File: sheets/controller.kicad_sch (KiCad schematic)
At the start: 40 parts, among them CN1 CTRL1, CN2 CTRL2, U12 74LS06

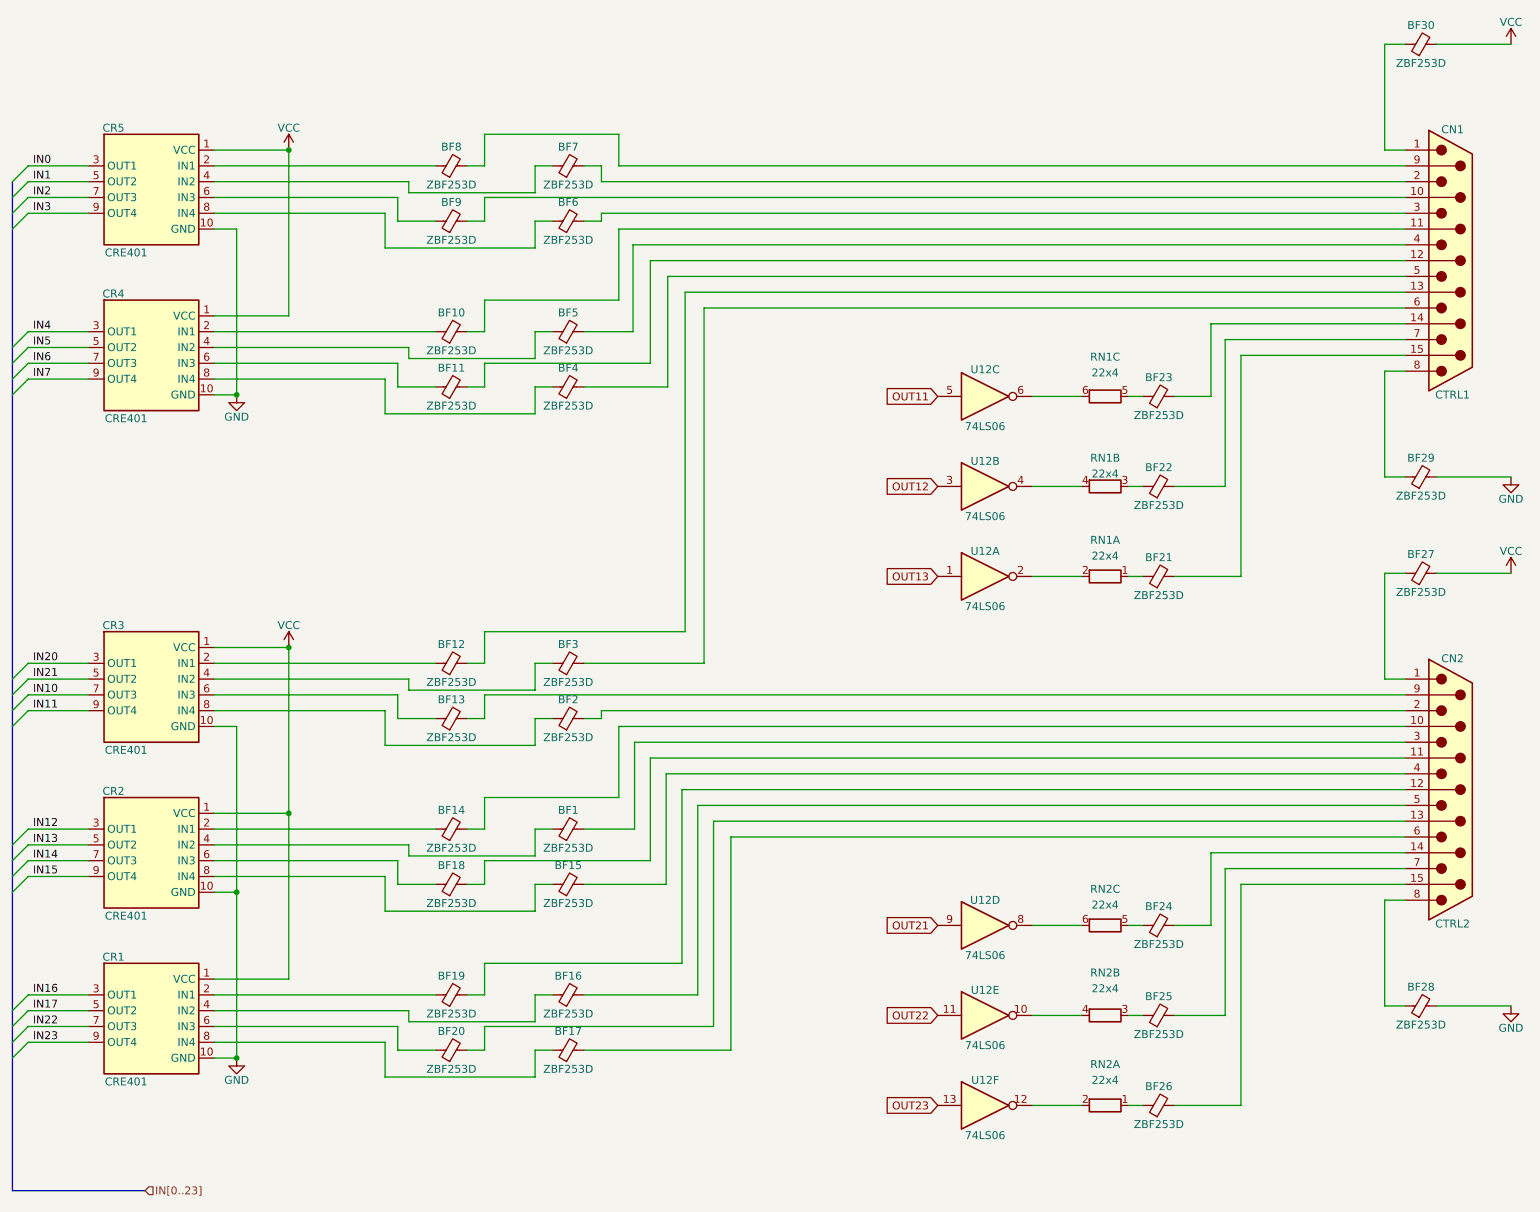
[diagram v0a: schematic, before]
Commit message: Updated to Kicad 10
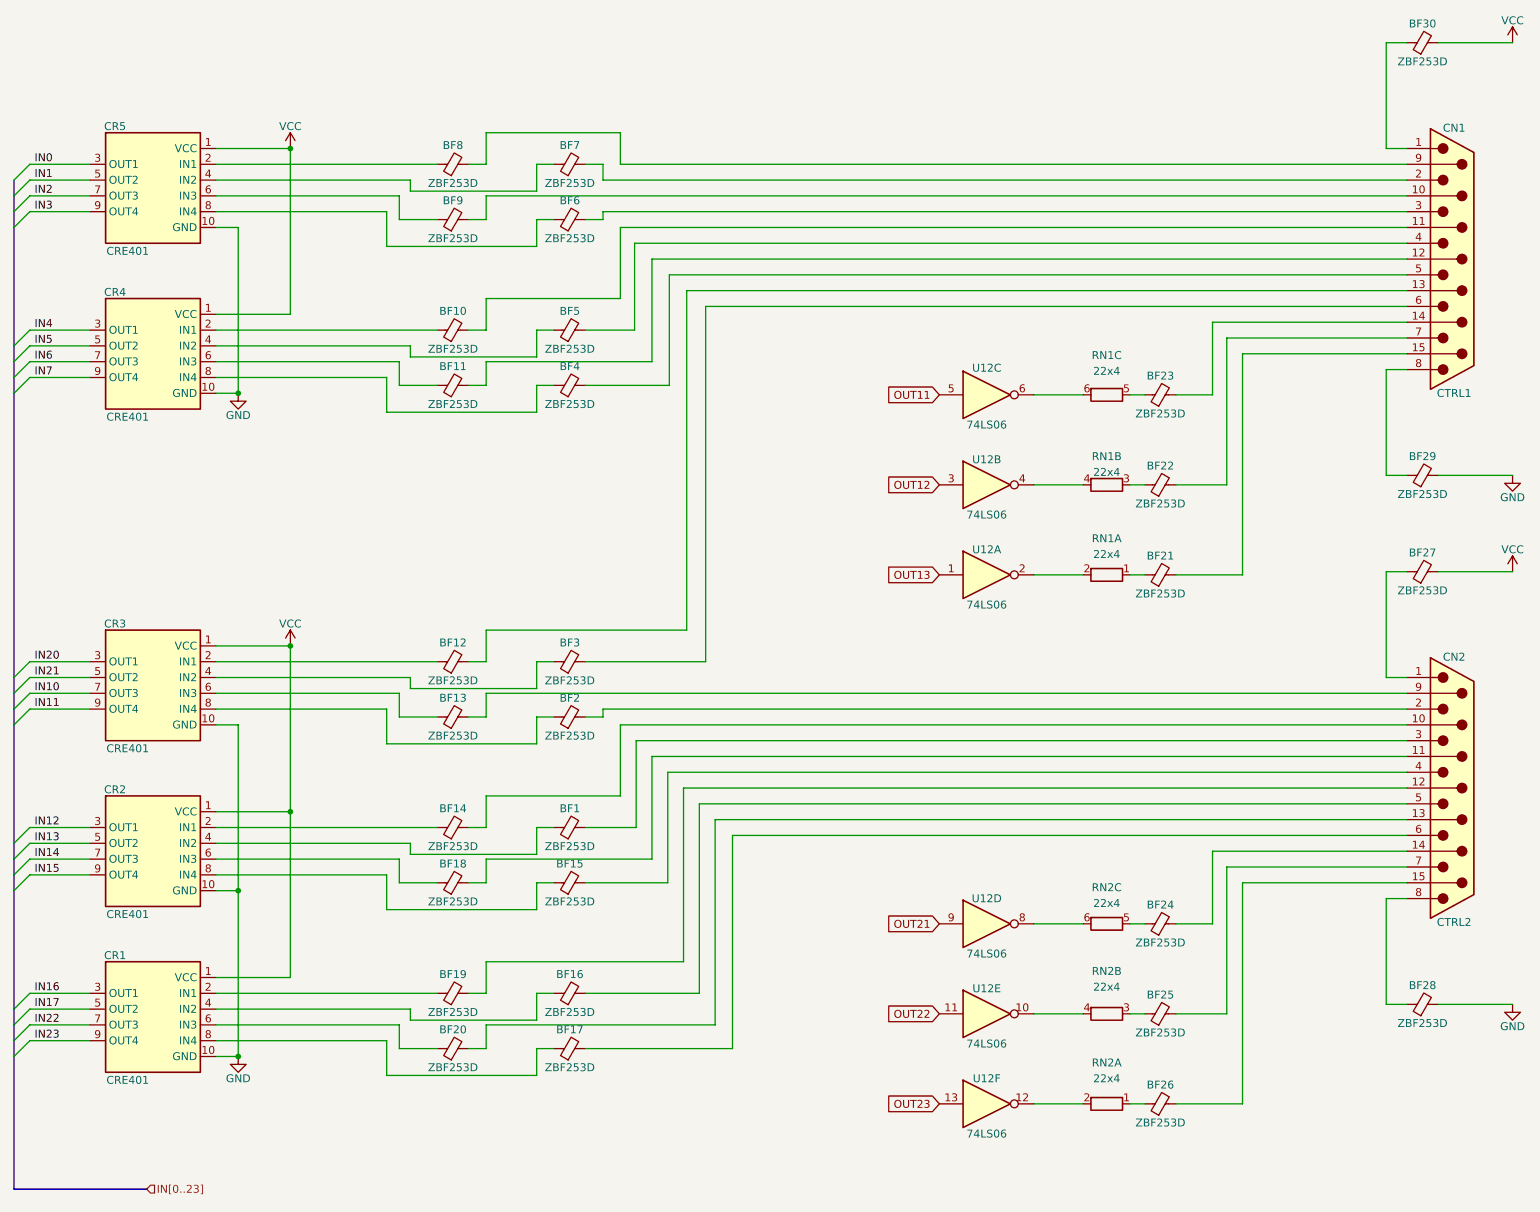
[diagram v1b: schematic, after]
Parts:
- CN1, CN2: symbol Connector:DA15_Plug -> Connector:DA15_Pins
